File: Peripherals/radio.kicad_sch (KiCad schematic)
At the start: 17 parts, among them U8 Si4468/7, Y2 26MHz

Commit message: Reorganised repo
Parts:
- AE1: value Antenna -> (none); footprint Connector_Coaxial:SMA_Molex_73251-2200_Horizontal -> (none)
- C21: value 100n -> (none); footprint Capacitor_SMD:C_0603_1608Metric -> (none)
- C22: value 5.1p -> (none); footprint Capacitor_SMD:C_0603_1608Metric -> (none)
- CM1: value 6.8n -> (none); footprint Capacitor_SMD:C_0603_1608Metric -> (none)
- CM2, CM3: value 3.3p -> (none); footprint Capacitor_SMD:C_0603_1608Metric -> (none)
- CR1: value 3p -> (none); footprint Capacitor_SMD:C_0603_1608Metric -> (none)
- CR2: value 1.2p -> (none); footprint Capacitor_SMD:C_0603_1608Metric -> (none)
- L1: value 3.3n -> (none); footprint Inductor_SMD:L_0603_1608Metric -> (none)
- LC1: value 120n -> (none); footprint Inductor_SMD:L_0603_1608Metric -> (none)
- LM1, LM3: value 12n -> (none); footprint Inductor_SMD:L_0603_1608Metric -> (none)
- LM2, LR2: value 24n -> (none); footprint Inductor_SMD:L_0603_1608Metric -> (none)
- LR1: value 18n -> (none); footprint Inductor_SMD:L_0603_1608Metric -> (none)
- U8: value Si4468/7 -> (none); footprint YAR_RF:SI4468-A2A-IMR -> (none)
- Y2: value 26MHz -> (none); footprint Oscillator:Oscillator_SMD_Abracon_ASE-4Pin_3.2x2.5mm -> (none)

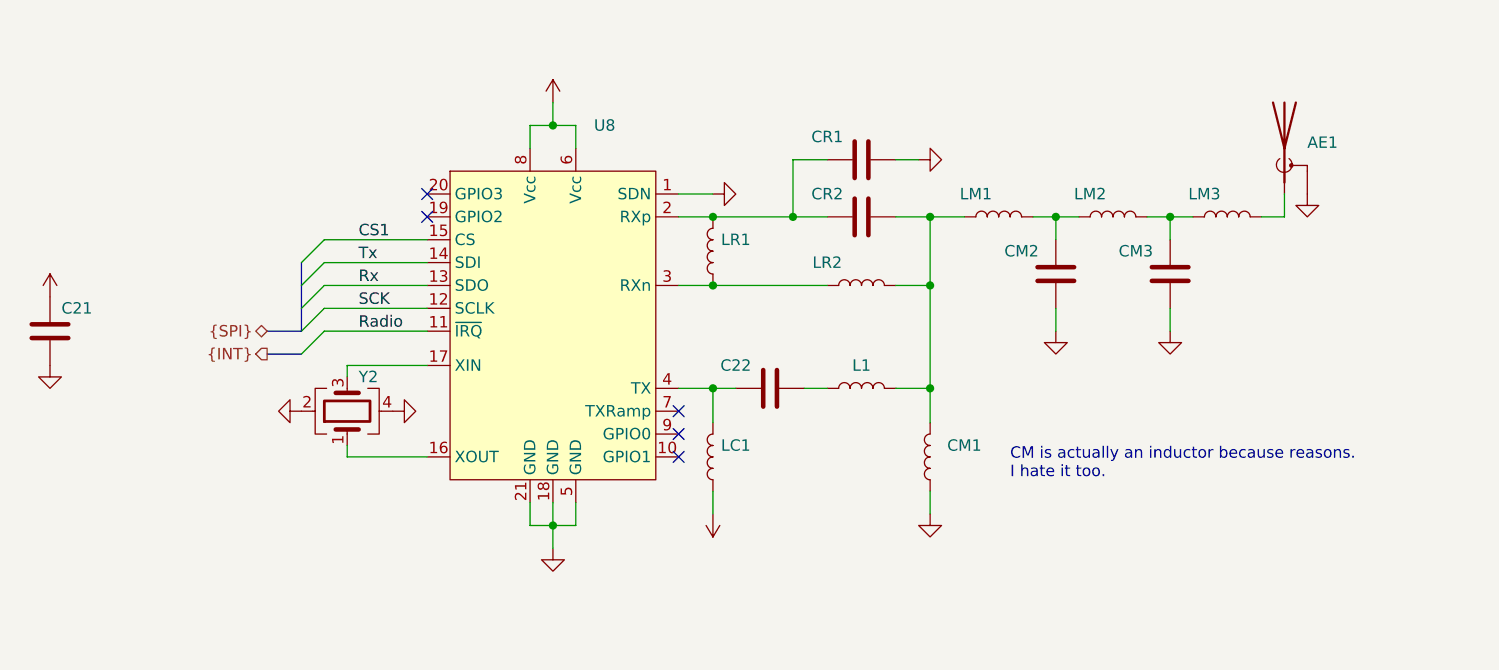
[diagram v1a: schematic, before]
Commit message: rev2 changes excluding pyro
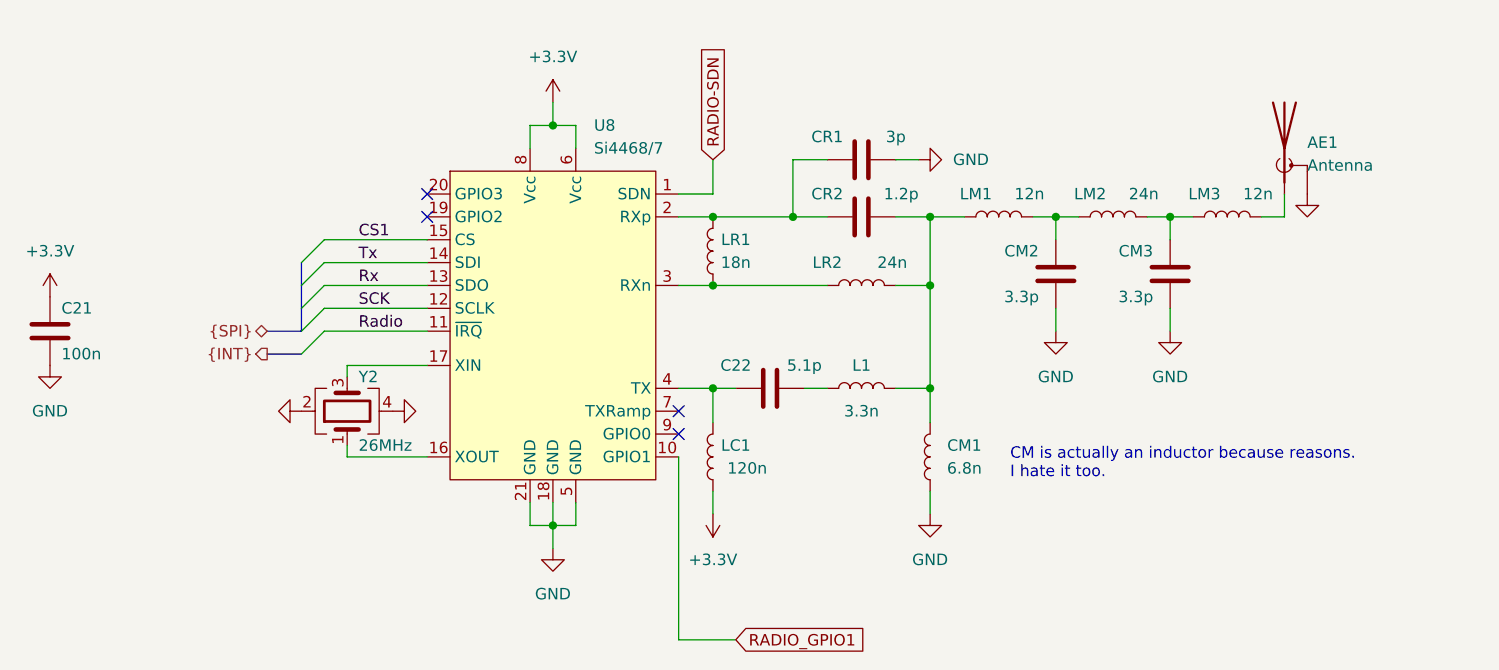
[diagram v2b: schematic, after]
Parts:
- AE1: value (none) -> Antenna; footprint (none) -> Connector_Coaxial:SMA_Molex_73251-2200_Horizontal
- C21: value (none) -> 100n; footprint (none) -> Capacitor_SMD:C_0603_1608Metric
- C22: value (none) -> 5.1p; footprint (none) -> Capacitor_SMD:C_0603_1608Metric
- CM1: value (none) -> 6.8n; footprint (none) -> Capacitor_SMD:C_0603_1608Metric
- CM2, CM3: value (none) -> 3.3p; footprint (none) -> Capacitor_SMD:C_0603_1608Metric
- CR1: value (none) -> 3p; footprint (none) -> Capacitor_SMD:C_0603_1608Metric
- CR2: value (none) -> 1.2p; footprint (none) -> Capacitor_SMD:C_0603_1608Metric
- L1: value (none) -> 3.3n; footprint (none) -> Inductor_SMD:L_0603_1608Metric
- LC1: value (none) -> 120n; footprint (none) -> Inductor_SMD:L_0603_1608Metric
- LM1, LM3: value (none) -> 12n; footprint (none) -> Inductor_SMD:L_0603_1608Metric
- LM2, LR2: value (none) -> 24n; footprint (none) -> Inductor_SMD:L_0603_1608Metric
- LR1: value (none) -> 18n; footprint (none) -> Inductor_SMD:L_0603_1608Metric
- U8: value (none) -> Si4468/7; footprint (none) -> YAR_RF:SI4468-A2A-IMR
- Y2: value (none) -> 26MHz; footprint (none) -> Oscillator:Oscillator_SMD_Abracon_ASE-4Pin_3.2x2.5mm
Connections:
- net GND: no longer U8.1 (SDN)
- net RADIO_GPIO1: now reaches U8.10 (GPIO1)
- new net RADIO-SDN: U8.1 (SDN)
- no-connect marks 5 -> 4
